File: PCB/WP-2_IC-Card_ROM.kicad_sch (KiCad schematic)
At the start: 6 parts, among them J1 SMS-138-01-G-S, SW1 Write-Enable, U1 29F0x0_TSOP

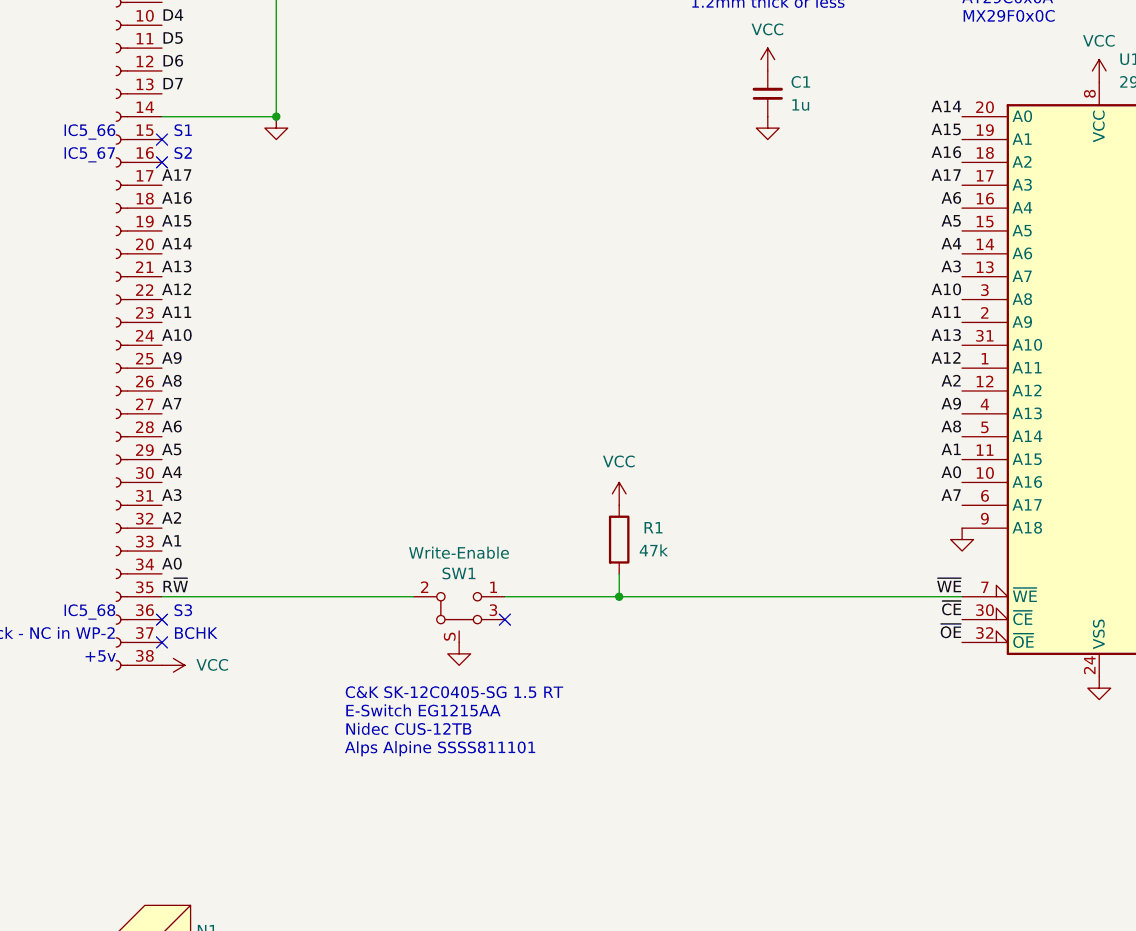
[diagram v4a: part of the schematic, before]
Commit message: update covers for flash & mram with bank sw & write sw
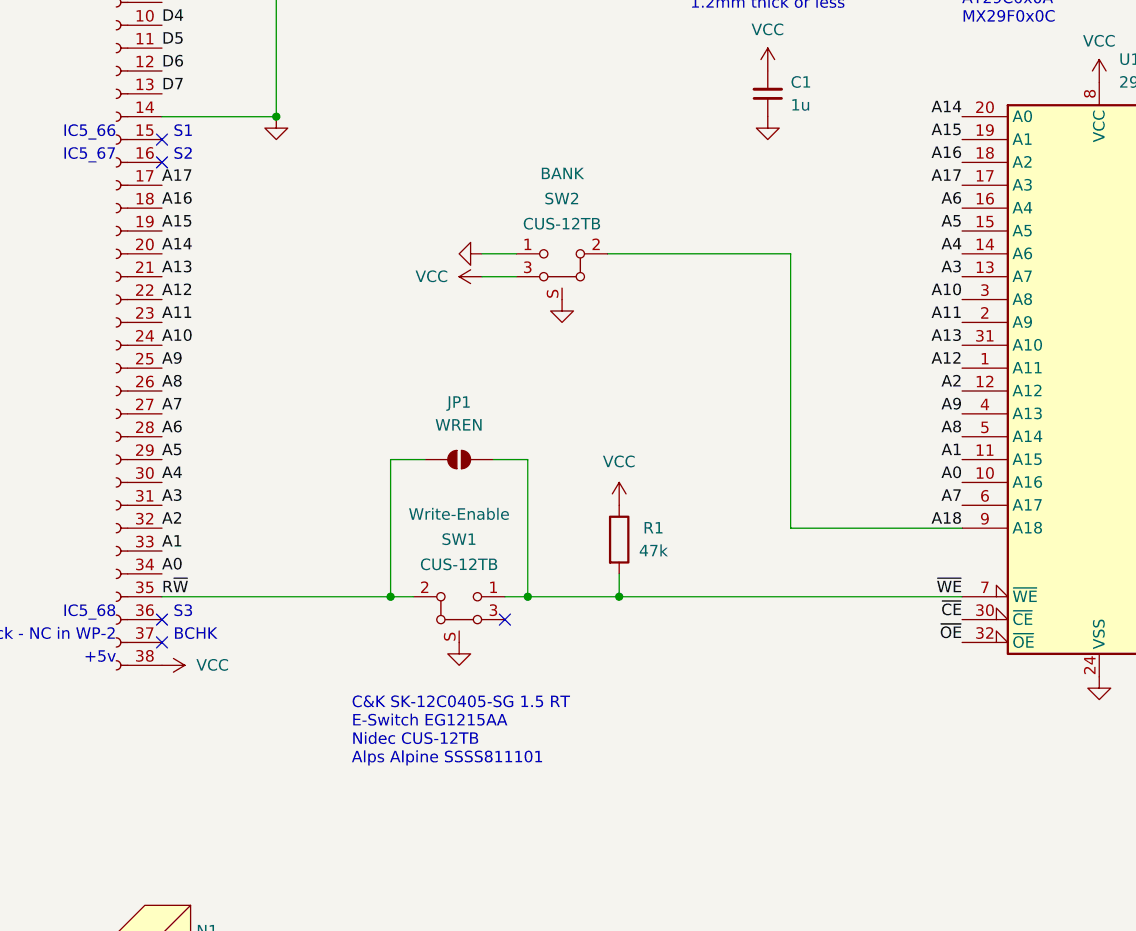
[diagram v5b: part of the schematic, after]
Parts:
- added JP1: WREN, 000_LOCAL:SolderJumper-2_open, symbol 000_LOCAL:SolderJumper_2_Open
- added SW2: CUS-12TB, 000_LOCAL:CUS-12TB pth, symbol 000_LOCAL:SW_SPDT_CUS-12
- SW1: value Write-Enable -> CUS-12TB; footprint 000_LOCAL:CUS-12TB pth -> 000_LOCAL:CUS-12TB slot pth; LABEL (none) -> Write-Enable
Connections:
- net GND: now also SW2.1, SW2.S; no longer U1.9 (A18)
- net R~{W}: now also JP1.1 (A)
- net VCC: now also SW2.3
- net ~{WE}: now also JP1.2 (B)
- new net A18: SW2.2 (C), U1.9 (A18)

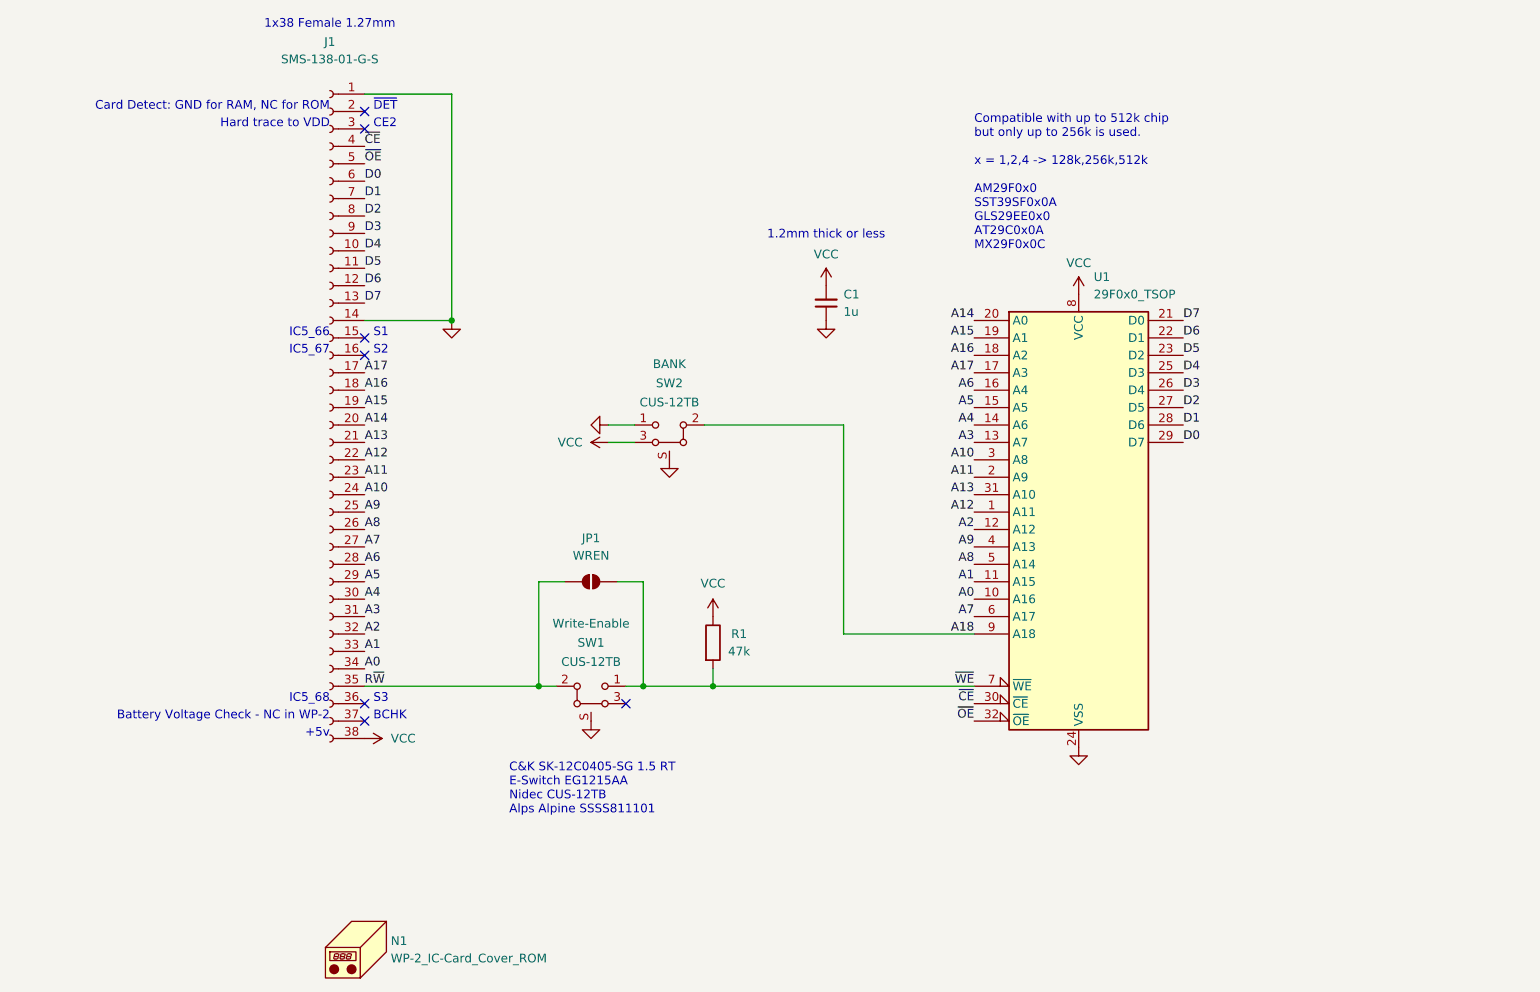
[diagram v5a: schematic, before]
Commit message: add resistor for A18 on rom card
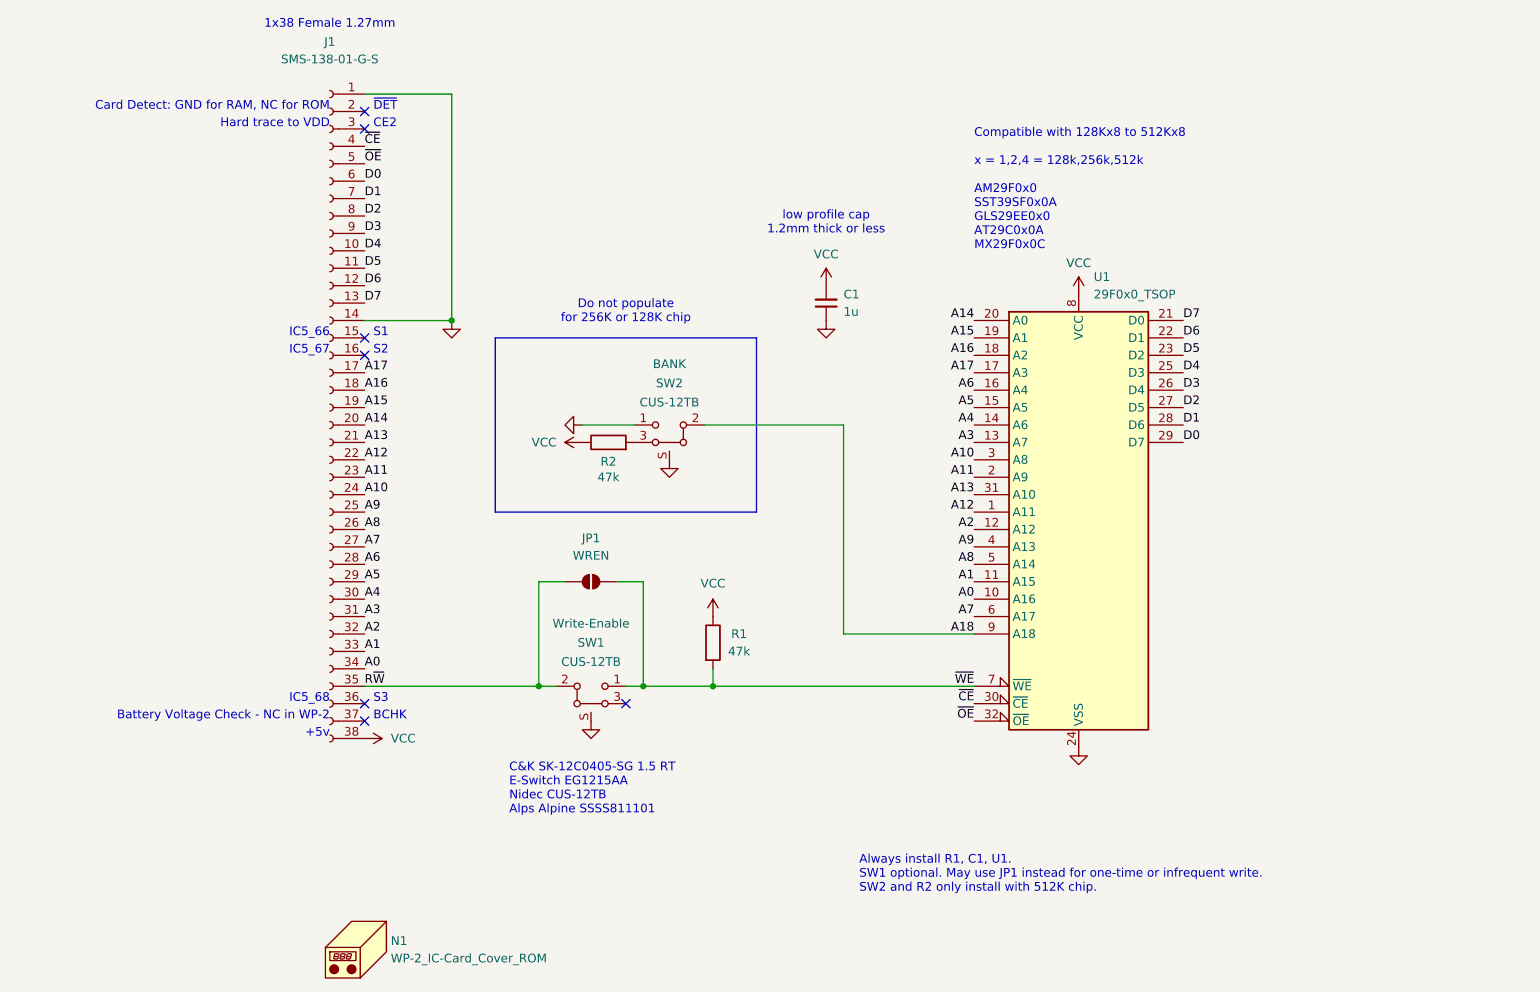
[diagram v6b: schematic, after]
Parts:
- added R2: 47k, 000_LOCAL:R_0805, symbol 000_LOCAL:R
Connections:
- net VCC: now also R2.1; no longer SW2.3
- new net: R2.2, SW2.3
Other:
- note added: "Always install R1, C1, U1. SW1 optional. May use JP1 instead for one-time or infrequent write. SW2 and R2 only install with 512K chip."
- note added: "Compatible with 128Kx8 to 512Kx8 x = 1,2,4 = 128k,256k,512k AM29F0x0 SST39SF0x0A GLS29EE0x0 AT29C0x0A MX29F0x0C"
- note added: "Do not populate for 256K or 128K chip"
- note added: "low profile cap 1.2mm thick or less"
- note removed: "1.2mm thick or less"
- note removed: "Compatible with up to 512k chip but only up to 256k is used. x = 1,2,4 -> 128k,256k,512k AM29F0x0 SST39SF0x0A GLS29EE0x0 AT29C0x0A MX29F0x0C"
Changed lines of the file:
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@@
 	(title_block
 		(title "WP-2_IC-Card_ROM")
-		(date "2025-04-17")
-		(rev "007")
+		(date "2025-04-20")
+		(rev "008")
 		(company "Brian K. White - b.kenyon.w@gmail.com")
 		(comment 1 "github.com/bkw777/WP-2_IC-Card")
@@
 	(wire
 		(pts
-			(xy 124.46 101.6) (xy 128.27 101.6)
+			(xy 120.65 101.6) (xy 128.27 101.6)
 		)
 		(stroke
@@
 	(wire
 		(pts
-			(xy 124.46 104.14) (xy 128.27 104.14)
+			(xy 101.6 86.36) (xy 101.6 53.34)
 		)
 		(stroke
@@
 	(wire
 		(pts
-			(xy 101.6 86.36) (xy 101.6 53.34)
+			(xy 125.73 124.46) (xy 129.54 124.46)
 		)
 		(stroke
@@
 	(wire
 		(pts
-			(xy 125.73 124.46) (xy 129.54 124.46)
+			(xy 127 139.7) (xy 129.54 139.7)
 		)
 		(stroke
@@
 	(wire
 		(pts
-			(xy 127 139.7) (xy 129.54 139.7)
+			(xy 88.9 53.34) (xy 101.6 53.34)
 		)
 		(stroke
@@
 	(wire
 		(pts
-			(xy 88.9 53.34) (xy 101.6 53.34)
+			(xy 88.9 139.7) (xy 114.3 139.7)
 		)
 		(stroke
@@
 	(wire
 		(pts
-			(xy 88.9 139.7) (xy 114.3 139.7)
+			(xy 129.54 124.46) (xy 129.54 139.7)
 		)
 		(stroke
@@
 		)
 	)
-	(wire
-		(pts
-			(xy 129.54 124.46) (xy 129.54 139.7)
-		)
+	(rectangle
+		(start 107.95 88.9)
+		(end 146.05 114.3)
 		(stroke
 			(width 0)
 			(type default)
 		)
-	)
-	(text "Compatible with up to 512k chip\nbut only up to 256k is used.\n\nx = 1,2,4 -> 128k,256k,512k\n\nAM29F0x0\nSST39SF0x0A\nGLS29EE0x0\nAT29C0x0A\nMX29F0x0C\n"
+		(fill
+			(type none)
+		)
+	)
+	(text "Compatible with 128Kx8 to 512Kx8\n\nx = 1,2,4 = 128k,256k,512k\n\nAM29F0x0\nSST39SF0x0A\nGLS29EE0x0\nAT29C0x0A\nMX29F0x0C\n"
 		(exclude_from_sim no)
 		(at 177.8 76.2 0)
@@
 		)
 	)
-	(text "1.2mm thick or less"
+	(text "low profile cap\n1.2mm thick or less"
 		(exclude_from_sim no)
 		(at 156.21 73.914 0)
@@
 				(size 1.27 1.27)
 			)
+			(justify bottom)
 		)
 	)
@@
 		)
 	)
+	(text "Always install R1, C1, U1.\nSW1 optional. May use JP1 instead for one-time or infrequent write.\nSW2 and R2 only install with 512K chip.\n"
+		(exclude_from_sim no)
+		(at 161.036 169.926 0)
+		(effects
+			(font
+				(size 1.27 1.27)
+			)
+			(justify left bottom)
+		)
+	)
 	(text "Battery Voltage Check - NC in WP-2"
 		(exclude_from_sim no)
@@
 		(exclude_from_sim no)
 		(at 83.82 43.18 0)
+		(effects
+			(font
+				(size 1.27 1.27)
+			)
+		)
+	)
+	(text "Do not populate\nfor 256K or 128K chip"
+		(exclude_from_sim no)
+		(at 127 85.09 0)
 		(effects
 			(font
@@
 	)
 	(symbol
+		(lib_id "000_LOCAL:R")
+		(at 124.46 104.14 90)
+		(unit 1)
+		(exclude_from_sim no)
+		(in_bom yes)
+		(on_board yes)
+		(dnp no)
+		(property "Reference" "R2"
+			(at 124.46 106.934 90)
+			(effects
+				(font
+					(size 1.27 1.27)
+				)
+			)
+		)
+		(property "Value" "47k"
+			(at 124.46 109.22 90)
+			(effects
+				(font
+					(size 1.27 1.27)
+				)
+			)
+		)
+		(property "Footprint" "000_LOCAL:R_0805"
+			(at 124.46 105.918 90)
+			(effects
+				(font
+					(size 1.27 1.27)
+				)
+				(hide yes)
+			)
+		)
+		(property "Datasheet" "datasheets/sei-rmcf_rmcp.pdf"
+			(at 124.46 104.14 0)
+			(effects
+				(font
+					(size 1.27 1.27)
+				)
+				(hide yes)
+			)
+		)
+		(property "Description" "RES 47K OHM 5% 1/8W 0805"
+			(at 124.46 104.14 0)
+			(effects
+				(font
+					(size 1.27 1.27)
+				)
+				(hide yes)
+			)
+		)
+		(property "MPN" "RMCF0805JT47K0"
+			(at 124.46 104.14 0)
+			(effects
+				(font
+					(size 1.27 1.27)
+				)
+				(hide yes)
+			)
+		)
+		(pin "1"
+		)
+		(pin "2"
+		)
+		(instances
+			(project "WP-2_IC-Card_ROM"
+				(path "/f291f000-461a-4127-8876-c8e21ea67ede"
+					(reference "R2")
+					(unit 1)
+				)
+			)
+		)
+	)
+	(symbol
 		(lib_id "power:GND")
 		(at 101.6 86.36 0)
@@
 	(symbol
 		(lib_id "power:GND")
-		(at 124.46 101.6 270)
+		(at 120.65 101.6 270)
 		(unit 1)
 		(exclude_from_sim no)
@@
 		(dnp no)
 		(property "Reference" "#PWR010"
-			(at 118.11 101.6 0)
+			(at 114.3 101.6 0)
 			(effects
 				(font
@@
 		)
 		(property "Value" "GND"
+			(at 116.84 101.6 0)
+			(effects
+				(font
+					(size 1.27 1.27)
+				)
+				(hide yes)
+			)
+		)
+		(property "Footprint" ""
 			(at 120.65 101.6 0)
 			(effects
@@
 			)
 		)
-		(property "Footprint" ""
-			(at 124.46 101.6 0)
-			(effects
-				(font
-					(size 1.27 1.27)
-				)
-				(hide yes)
-			)
-		)
 		(property "Datasheet" ""
-			(at 124.46 101.6 0)
+			(at 120.65 101.6 0)
 			(effects
 				(font
@@
 		)
 		(property "Description" ""
-			(at 124.46 101.6 0)
+			(at 120.65 101.6 0)
 			(effects
 				(font
@@
 	(symbol
 		(lib_id "000_LOCAL:VCC")
-		(at 124.46 104.14 90)
+		(at 120.65 104.14 90)
 		(unit 1)
 		(exclude_from_sim no)
@@
 		(dnp no)
 		(property "Reference" "#PWR04"
-			(at 128.27 104.14 0)
+			(at 124.46 104.14 0)
 			(effects
 				(font
@@
 		)
 		(property "Value" "VCC"
-			(at 118.872 104.14 90)
+			(at 115.062 104.14 90)
 			(effects
 				(font
@@
 		)
 		(property "Footprint" ""
-			(at 124.46 104.14 0)
+			(at 120.65 104.14 0)
 			(effects
 				(font
@@
 		)
 		(property "Datasheet" ""
-			(at 124.46 104.14 0)
+			(at 120.65 104.14 0)
 			(effects
 				(font
@@
 		)
 		(property "Description" "Power symbol creates a global label with name \"VCC\""
-			(at 124.46 104.14 0)
-			(effects
-				(font
+			(at 120.65 104.14 0)
+			(effects
+				(font
